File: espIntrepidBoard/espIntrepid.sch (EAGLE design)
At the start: 24 parts, among them Q1 TRANS_NPN, Q2 TRANS_NPN, Q3 TRANS_NPN, Q4 TRANS_PNP, Q5 TRANS_PNP, Q6 TRANS_PNP, Q7 TRANS_NPN, U1 ESP32DEV_38, U2 MOSFET_P, U3 MOSFET_P, U4 MOSFET_P

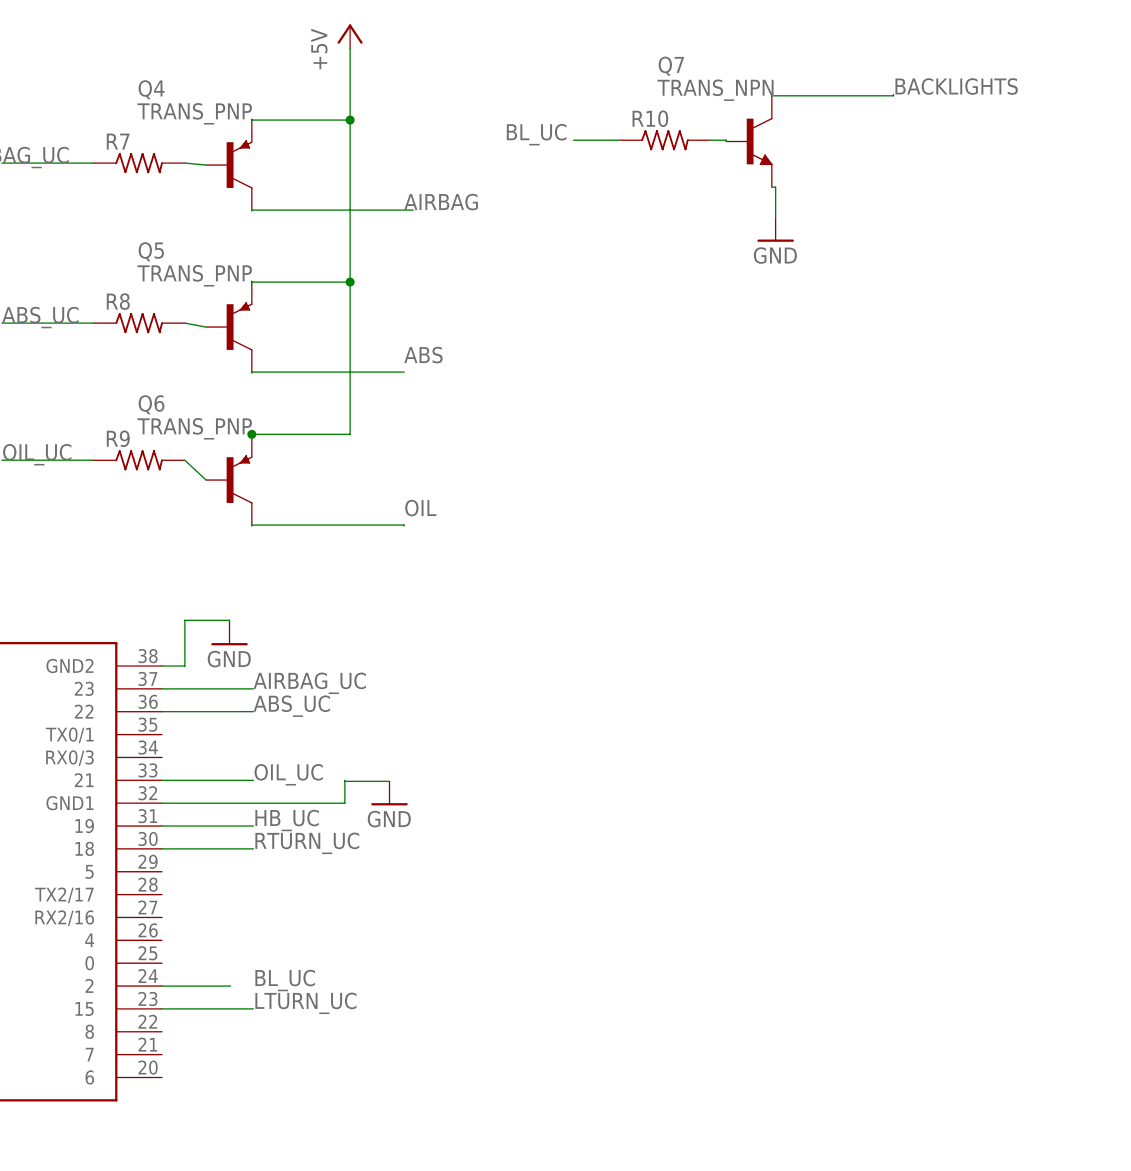
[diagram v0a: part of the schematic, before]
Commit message: Started board routing
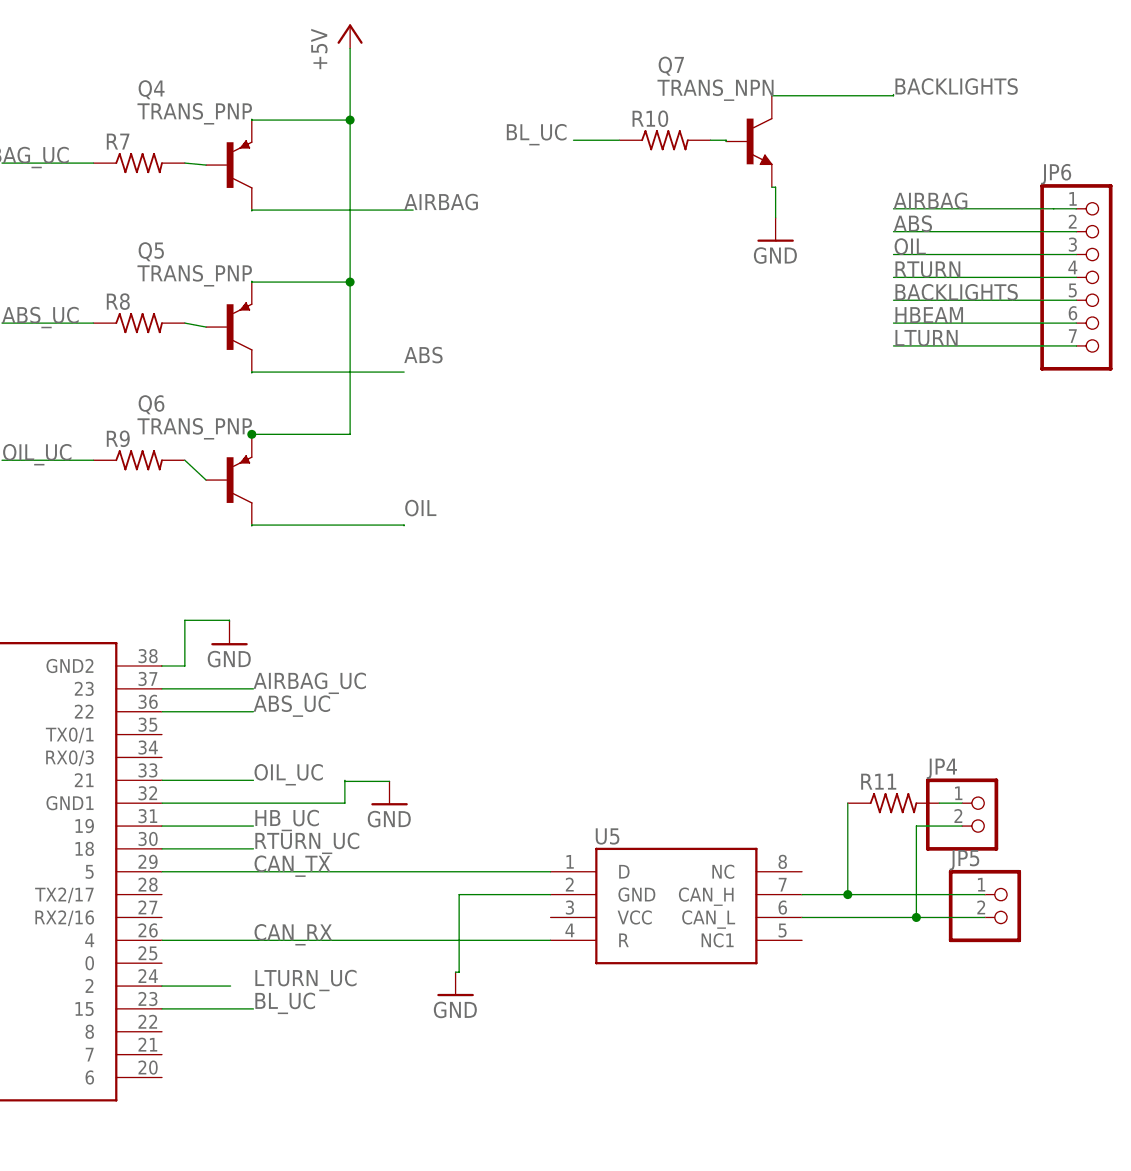
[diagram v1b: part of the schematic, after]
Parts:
- added JP4, JP5: (no value), pinhead:PINHD-1X2
- added JP6: (no value), pinhead:PINHD-1X7
- added R11: (no value), DR:R-US_M1206
- added U5: SN65HVD232DSOIC8, DR:SN65HVD232DSOIC8
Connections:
- new net CAN_RX: U1.4, U5.R
- new net CAN_TX: U1.5, U5.D
- new net N$19: JP4.2, JP5.2, U5.CAN_L
- new net N$21: JP4.1, R11.2
- new net N$3: JP5.1, R11.1, U5.CAN_H
- net ABS: now also JP6.2
- net AIRBAG: now also JP6.1
- net BACKLIGHTS: now also JP6.5
- net BL_UC: now also U1.15; no longer U1.2
- net GND: now also U5.GND
- net HBEAM: now also JP6.6
- net LTURN: now also JP6.7
- net LTURN_UC: now also U1.2; no longer U1.15
- net OIL: now also JP6.3
- net RTURN: now also JP6.4
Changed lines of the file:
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@@
 <part name="R10" library="DR" deviceset="R-US_" device="M1206"/>
 <part name="GND8" library="supply1" deviceset="GND" device=""/>
+<part name="U5" library="DR" deviceset="SN65HVD232D" device="SOIC8"/>
+<part name="GND9" library="supply1" deviceset="GND" device=""/>
+<part name="R11" library="DR" deviceset="R-US_" device="M1206"/>
+<part name="JP4" library="pinhead" library_urn="urn:adsk.eagle:library:325" deviceset="PINHD-1X2" device="" package3d_urn="urn:adsk.eagle:package:22435/2"/>
+<part name="JP5" library="pinhead" library_urn="urn:adsk.eagle:library:325" deviceset="PINHD-1X2" device="" package3d_urn="urn:adsk.eagle:package:22435/2"/>
+<part name="JP6" library="pinhead" library_urn="urn:adsk.eagle:library:325" deviceset="PINHD-1X7" device="" package3d_urn="urn:adsk.eagle:package:22477/2"/>
 </parts>
 <sheets>
@@
 <attribute name="VALUE" x="205.34" y="100.6" size="1.778" layer="96"/>
 </instance>
+<instance part="U5" gate="G$1" x="182.88" y="33.02" smashed="yes">
+<attribute name="NAME" x="187.706" y="36.068" size="1.778" layer="95"/>
+</instance>
+<instance part="GND9" gate="1" x="172.32" y="19.32" smashed="yes">
+<attribute name="VALUE" x="169.78" y="16.78" size="1.778" layer="96"/>
+</instance>
+<instance part="R11" gate="G$1" x="220.98" y="40.64" smashed="yes">
+<attribute name="NAME" x="217.17" y="42.1386" size="1.778" layer="95"/>
+<attribute name="VALUE" x="217.17" y="37.338" size="1.778" layer="96"/>
+</instance>
+<instance part="JP4" gate="G$1" x="231.14" y="38.1" smashed="yes">
+<attribute name="NAME" x="224.79" y="43.815" size="1.778" layer="95"/>
+<attribute name="VALUE" x="224.79" y="33.02" size="1.778" layer="96"/>
+</instance>
+<instance part="JP5" gate="G$1" x="233.68" y="27.94" smashed="yes">
+<attribute name="NAME" x="227.33" y="33.655" size="1.778" layer="95"/>
+<attribute name="VALUE" x="227.33" y="22.86" size="1.778" layer="96"/>
+</instance>
+<instance part="JP6" gate="A" x="243.84" y="99.06" smashed="yes">
+<attribute name="NAME" x="237.49" y="109.855" size="1.778" layer="95"/>
+<attribute name="VALUE" x="237.49" y="86.36" size="1.778" layer="96"/>
+</instance>
 </instances>
 <busses>
@@
 <wire x1="207.46" y1="109.08" x2="207.88" y2="109.08" width="0.1524" layer="91"/>
 <wire x1="207.88" y1="109.08" x2="207.88" y2="105.68" width="0.1524" layer="91"/>
+</segment>
+<segment>
+<pinref part="U5" gate="G$1" pin="GND"/>
+<wire x1="182.88" y1="30.48" x2="172.72" y2="30.48" width="0.1524" layer="91"/>
+<pinref part="GND9" gate="1" pin="GND"/>
+<wire x1="172.72" y1="30.48" x2="172.72" y2="21.86" width="0.1524" layer="91"/>
+<wire x1="172.72" y1="21.86" x2="172.32" y2="21.86" width="0.1524" layer="91"/>
 </segment>
 </net>
@@
 <wire x1="102.6" y1="100.92" x2="102.6" y2="99.54" width="0.1524" layer="91"/>
 </segment>
+<segment>
+<wire x1="220.98" y1="99.06" x2="241.3" y2="99.06" width="0.1524" layer="91"/>
+<pinref part="JP6" gate="A" pin="4"/>
+<label x="220.98" y="99.06" size="1.778" layer="95"/>
+</segment>
 </net>
 <net name="LTURN" class="0">
@@
 <wire x1="86.68" y1="82.92" x2="86.68" y2="81.54" width="0.1524" layer="91"/>
 <wire x1="86.68" y1="81.54" x2="102.6" y2="81.54" width="0.1524" layer="91"/>
+</segment>
+<segment>
+<wire x1="220.98" y1="91.44" x2="241.3" y2="91.44" width="0.1524" layer="91"/>
+<label x="220.98" y="91.44" size="1.778" layer="95"/>
+<pinref part="JP6" gate="A" pin="7"/>
 </segment>
 </net>
@@
 <wire x1="102.6" y1="66.54" x2="101.6" y2="66.54" width="0.1524" layer="91"/>
 </segment>
+<segment>
+<wire x1="220.98" y1="93.98" x2="241.3" y2="93.98" width="0.1524" layer="91"/>
+<pinref part="JP6" gate="A" pin="6"/>
+<label x="220.98" y="93.98" size="1.778" layer="95"/>
+</segment>
 </net>
 <net name="N$11" class="0">
@@
 <wire x1="149.68" y1="106.54" x2="149.68" y2="106.46" width="0.1524" layer="91"/>
 </segment>
+<segment>
+<pinref part="JP6" gate="A" pin="1"/>
+<wire x1="238.76" y1="106.68" x2="241.3" y2="106.68" width="0.1524" layer="91"/>
+<wire x1="238.76" y1="106.68" x2="220.98" y2="106.68" width="0.1524" layer="91"/>
+<label x="220.98" y="106.68" size="1.778" layer="95"/>
+</segment>
 </net>
 <net name="ABS" class="0">
@@
 <wire x1="166.6" y1="88.54" x2="149.68" y2="88.54" width="0.1524" layer="91"/>
 <wire x1="149.68" y1="88.54" x2="149.68" y2="88.46" width="0.1524" layer="91"/>
+</segment>
+<segment>
+<wire x1="241.3" y1="104.14" x2="220.98" y2="104.14" width="0.1524" layer="91"/>
+<pinref part="JP6" gate="A" pin="2"/>
+<label x="220.98" y="104.14" size="1.778" layer="95"/>
 </segment>
 </net>
@@
 <wire x1="149.68" y1="71.54" x2="149.68" y2="71.46" width="0.1524" layer="91"/>
 </segment>
+<segment>
+<wire x1="241.3" y1="101.6" x2="220.98" y2="101.6" width="0.1524" layer="91"/>
+<pinref part="JP6" gate="A" pin="3"/>
+<label x="220.98" y="101.6" size="1.778" layer="95"/>
+</segment>
 </net>
 <net name="N$22" class="0">
@@
 <net name="LTURN_UC" class="0">
 <segment>
-<wire x1="139.7" y1="17.78" x2="149.86" y2="17.78" width="0.1524" layer="91"/>
-<label x="149.86" y="17.78" size="1.778" layer="95"/>
-<pinref part="U1" gate="G$1" pin="15"/>
-</segment>
-<segment>
 <wire x1="22.86" y1="76.2" x2="43.18" y2="76.2" width="0.1524" layer="91"/>
 <label x="22.86" y="76.2" size="1.778" layer="95"/>
 <pinref part="R6" gate="G$1" pin="1"/>
+</segment>
+<segment>
+<wire x1="147.32" y1="20.32" x2="139.7" y2="20.32" width="0.1524" layer="91"/>
+<pinref part="U1" gate="G$1" pin="2"/>
+<label x="149.86" y="20.32" size="1.778" layer="95"/>
 </segment>
 </net>
@@
 <label x="220.98" y="119.38" size="1.778" layer="95"/>
 </segment>
+<segment>
+<wire x1="220.98" y1="96.52" x2="241.3" y2="96.52" width="0.1524" layer="91"/>
+<label x="220.98" y="96.52" size="1.778" layer="95"/>
+<pinref part="JP6" gate="A" pin="5"/>
+</segment>
 </net>
 <net name="BL_UC" class="0">
@@
 </segment>
 <segment>
-<wire x1="147.32" y1="20.32" x2="139.7" y2="20.32" width="0.1524" layer="91"/>
-<pinref part="U1" gate="G$1" pin="2"/>
-<label x="149.86" y="20.32" size="1.778" layer="95"/>
+<wire x1="139.7" y1="17.78" x2="149.86" y2="17.78" width="0.1524" layer="91"/>
+<label x="149.86" y="17.78" size="1.778" layer="95"/>
+<pinref part="U1" gate="G$1" pin="15"/>
+</segment>
+</net>
+<net name="CAN_RX" class="0">
+<segment>
+<pinref part="U1" gate="G$1" pin="4"/>
+<label x="149.86" y="25.4" size="1.778" layer="95"/>
+<pinref part="U5" gate="G$1" pin="R"/>
+<wire x1="139.7" y1="25.4" x2="182.88" y2="25.4" width="0.1524" layer="91"/>
+</segment>
+</net>
+<net name="CAN_TX" class="0">
+<segment>
+<pinref part="U1" gate="G$1" pin="5"/>
+<label x="149.86" y="33.02" size="1.778" layer="95"/>
+<pinref part="U5" gate="G$1" pin="D"/>
+<wire x1="182.88" y1="33.02" x2="139.7" y2="33.02" width="0.1524" layer="91"/>
+</segment>
+</net>
+<net name="N$3" class="0">
+<segment>
+<pinref part="U5" gate="G$1" pin="CAN_H"/>
+<wire x1="210.82" y1="30.48" x2="215.9" y2="30.48" width="0.1524" layer="91"/>
+<pinref part="R11" gate="G$1" pin="1"/>
+<wire x1="215.9" y1="30.48" x2="231.14" y2="30.48" width="0.1524" layer="91"/>
+<wire x1="215.9" y1="40.64" x2="215.9" y2="30.48" width="0.1524" layer="91"/>
+<junction x="215.9" y="30.48"/>
+<pinref part="JP5" gate="G$1" pin="1"/>
+</segment>
+</net>
+<net name="N$19" class="0">
+<segment>
+<pinref part="U5" gate="G$1" pin="CAN_L"/>
+<wire x1="210.82" y1="27.94" x2="223.52" y2="27.94" width="0.1524" layer="91"/>
+<pinref part="JP4" gate="G$1" pin="2"/>
+<wire x1="223.52" y1="27.94" x2="231.14" y2="27.94" width="0.1524" layer="91"/>
+<wire x1="228.6" y1="38.1" x2="223.52" y2="38.1" width="0.1524" layer="91"/>
+<wire x1="223.52" y1="38.1" x2="223.52" y2="27.94" width="0.1524" layer="91"/>
+<junction x="223.52" y="27.94"/>
+<pinref part="JP5" gate="G$1" pin="2"/>
+</segment>
+</net>
+<net name="N$21" class="0">
+<segment>
+<pinref part="JP4" gate="G$1" pin="1"/>
+<pinref part="R11" gate="G$1" pin="2"/>
+<wire x1="228.6" y1="40.64" x2="226.06" y2="40.64" width="0.1524" layer="91"/>
 </segment>
 </net>
@@
 which will not be processed correctly with this version.
 </note>
+<note version="8.2" severity="warning">
+Since Version 8.2, EAGLE supports online libraries. The ids
+of those online libraries will not be understood (or retained)
+with this version.
+</note>
+<note version="8.3" severity="warning">
+Since Version 8.3, EAGLE supports URNs for individual library
+assets (packages, symbols, and devices). The URNs of those assets
+will not be understood (or retained) with this version.
+</note>
+<note version="8.3" severity="warning">
+Since Version 8.3, EAGLE supports the association of 3D packages
+with devices in libraries, schematics, and board files. Those 3D
+packages will not be understood (or retained) with this version.
+</note>
 </compatibility>

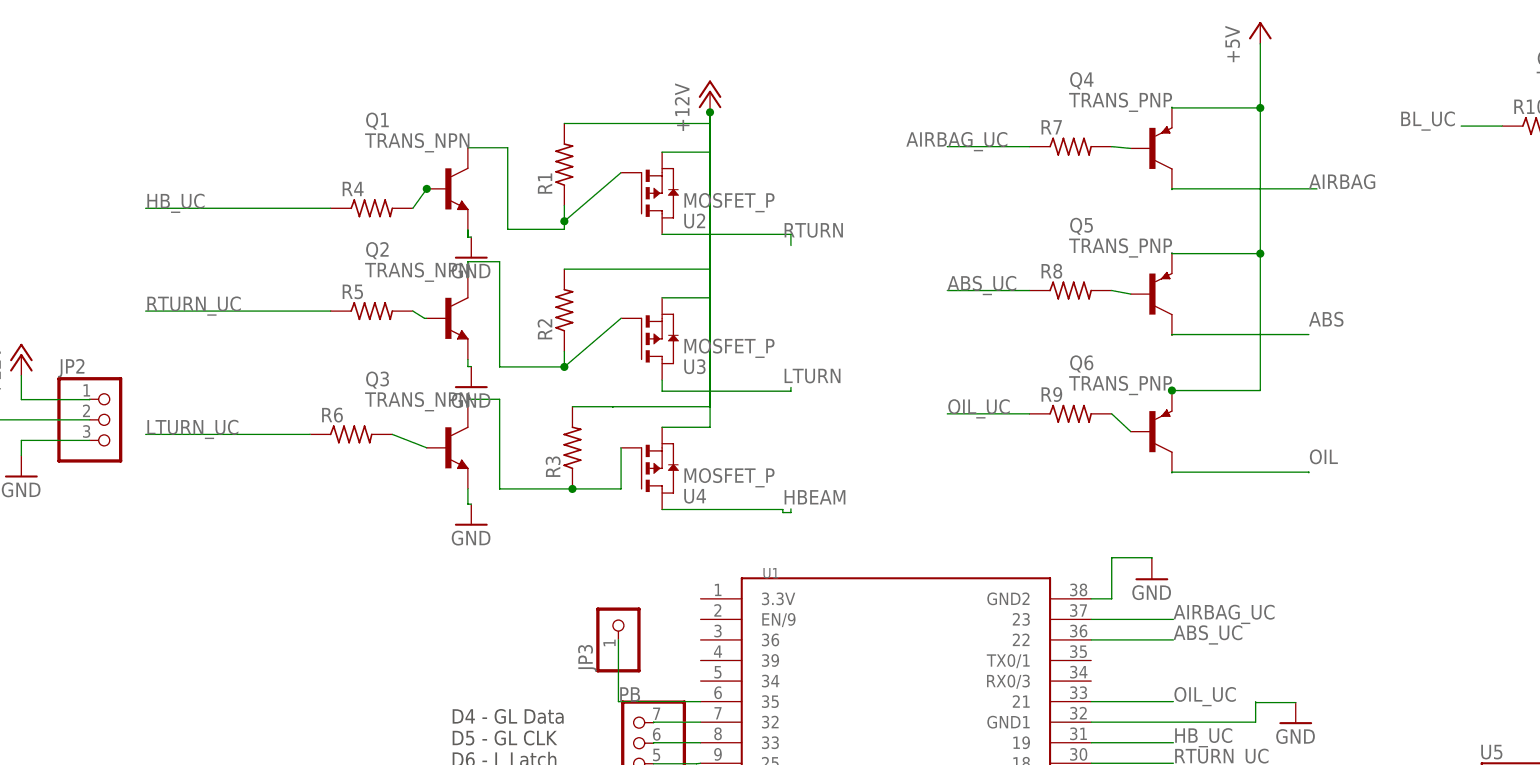
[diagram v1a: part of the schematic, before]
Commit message: Using optoisolators
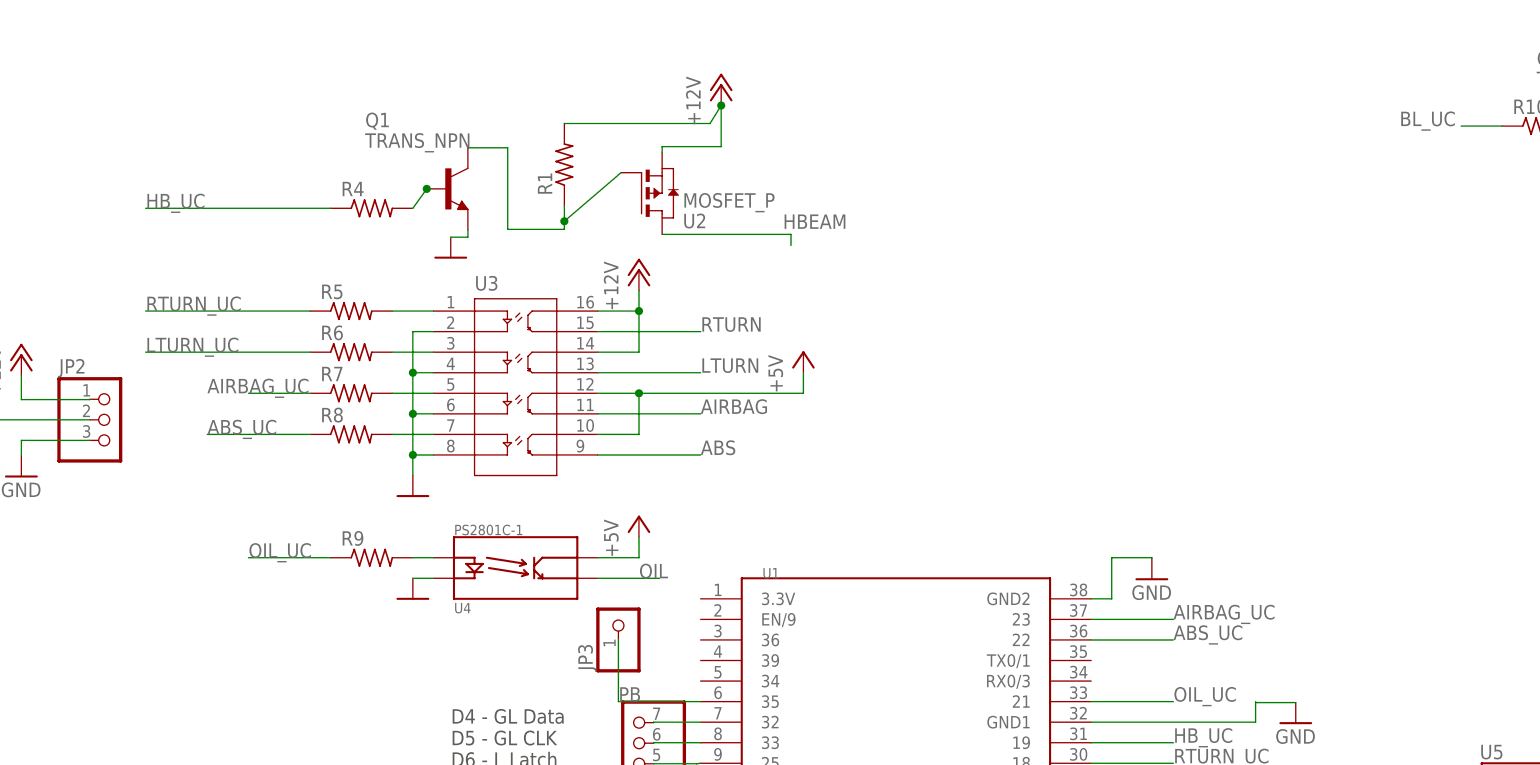
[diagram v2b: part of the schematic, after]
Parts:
- removed Q2, Q3: TRANS_NPN, DR:TRANS_NPN
- removed Q4, Q5, Q6: TRANS_PNP, DR:TRANS_PNP
- removed R2, R3: (no value), DR:R-US_M1206
- U3: value MOSFET_P -> LTV-847; device DR:MOSFET_P -> DR:LTV-847
- U4: value MOSFET_P -> PS2801C-1; device DR:MOSFET_P -> SureFireParts 6.0:PS2801C-1
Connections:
- removed net N$16: Q3.C, R3.1, U4.G
- removed net N$22: Q4.B, R7.2
- removed net N$23: Q5.B, R8.2
- removed net N$24: Q6.B, R9.2
- new net N$15: R7.2, U3.P$5
- new net N$2: R5.2, U3.P$1
- net +12V: now also U3.P$14, U3.P$16; no longer R2.2, R3.2, U3.S, U4.S
- net +5V: now also U3.P$10, U3.P$12, U4.4; no longer Q4.E, Q5.E, Q6.E
- net ABS: now also U3.P$9; no longer Q5.C
- net AIRBAG: now also U3.P$11; no longer Q4.C
- net GND: now also U3.P$2, U3.P$4, U3.P$6, U3.P$8, U4.2; no longer Q2.E, Q3.E
- net HBEAM: now also U2.D; no longer U4.D
- net LTURN: now also U3.P$13; no longer U3.D
- net N$11: now also R8.2, U3.P$7; no longer Q2.B, R5.2
- net N$14: now also R6.2, U3.P$3; no longer Q2.C, R2.1, U3.G
- net N$17: now also R9.2, U4.1; no longer Q3.B, R6.2
- net OIL: now also U4.3; no longer Q6.C
- net RTURN: now also U3.P$15; no longer U2.D
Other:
- moved on the sheet: R5, R6, R7, R8, R9
